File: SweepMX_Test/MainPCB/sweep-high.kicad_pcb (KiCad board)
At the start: 2 copper layers, 229.5 x 95.2 mm, 61 parts, among them J1 AudioJack4dpb, J2 AudioJack4dpb, SW10 SW_Push, SW10_r1 SW_Push, SW11 SW_Push, SW11_r1 SW_Push, SW12 SW_Push, SW12_r1 SW_Push, SW14 SW_Push, SW14_r1 SW_Push, SW15 SW_Push, SW15_r1 SW_Push, SW16 SW_Push, SW16_r1 SW_Push, SW17 SW_Push, SW17_r1 SW_Push, SW18 SW_Push, SW18_r1 SW_Push, SW2 SW_Push, SW20 SW_Push, SW20_r1 SW_Push, SW21 SW_Push, SW21_r1 SW_Push, SW2_r1 SW_Push, SW3 SW_Push, SW3_r1 SW_Push, SW4 SW_Push, SW4_r1 SW_Push, SW5 SW_Push, SW5_r1 SW_Push, SW6 SW_Push, SW6_r1 SW_Push, SW8 SW_Push, SW8_r1 SW_Push, SW9 SW_Push, SW9_r1 SW_Push, U1 ProMicro-kbd, U2 ProMicro-kbd

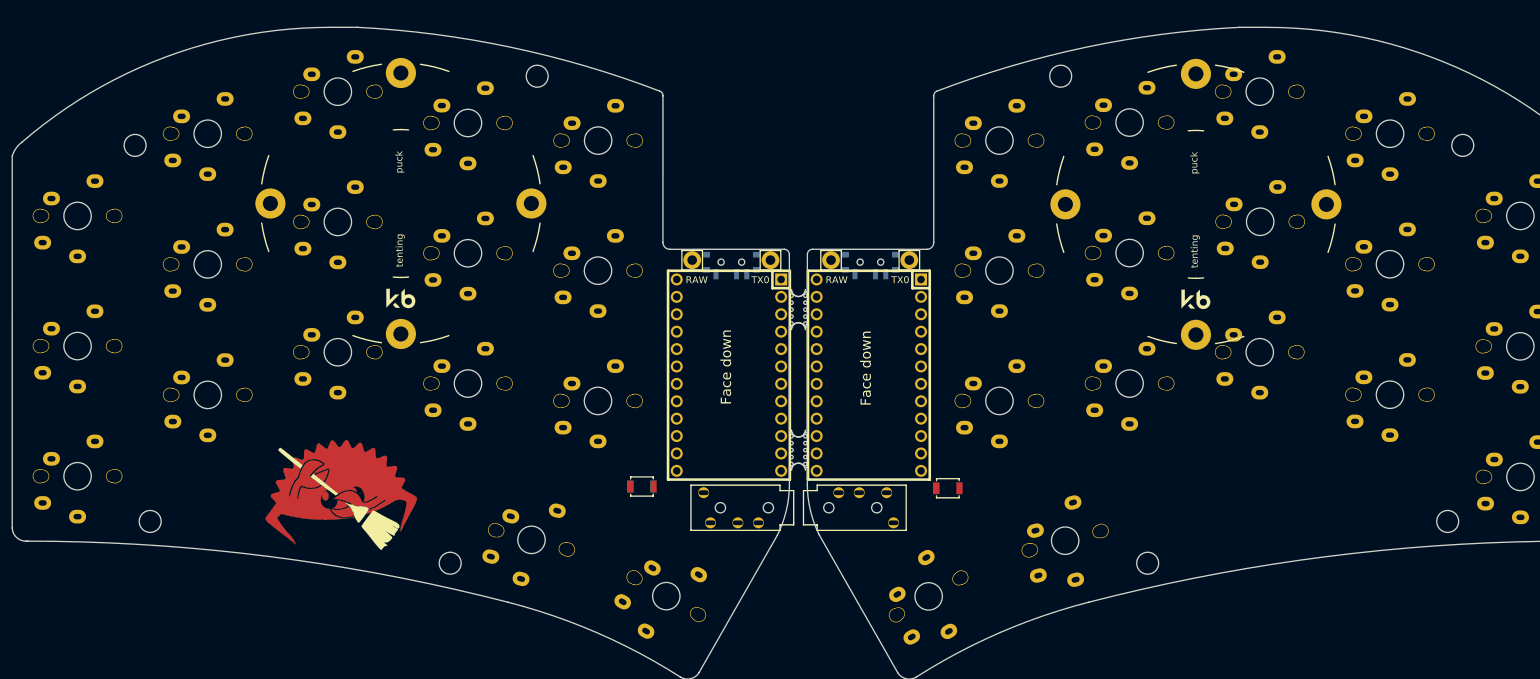
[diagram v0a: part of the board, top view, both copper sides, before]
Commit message: routed all traces on MX version with matching pinout to PR
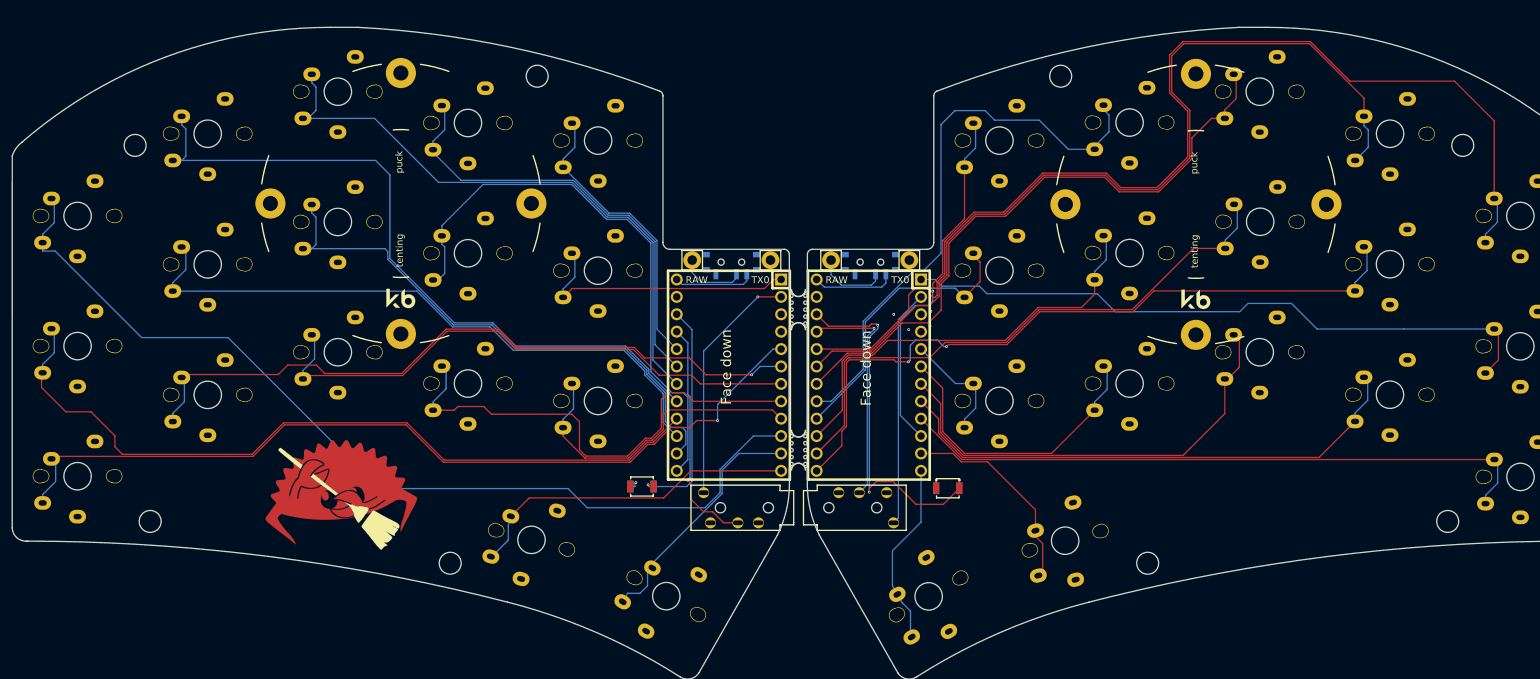
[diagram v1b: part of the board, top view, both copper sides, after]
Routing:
- net Switch1_r: track 0.00 -> 161.8 mm
- net Switch1: track 0.00 -> 138.2 mm
- net Switch2_r: track 0.00 -> 131.0 mm
- net Switch11: track 0.00 -> 126.5 mm, vias 0 -> 1
- net Switch6: track 0.00 -> 113.9 mm
- net Switch7_r: track 0.00 -> 105.8 mm, vias 0 -> 2
- net Switch2: track 0.00 -> 102.6 mm
- net Switch12: track 0.00 -> 102.0 mm, vias 0 -> 1
- net Switch6_r: track 0.00 -> 95.1 mm
- net Switch11_r: track 0.00 -> 93.5 mm
- net Switch7: track 0.00 -> 92.6 mm
- net Switch3_r: track 0.00 -> 91.5 mm
- net Switch3: track 0.00 -> 88.6 mm
- net Switch8_r: track 0.00 -> 84.9 mm
- net Switch4_r: track 0.00 -> 83.2 mm
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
